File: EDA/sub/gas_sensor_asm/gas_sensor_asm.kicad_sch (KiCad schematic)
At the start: 13 parts, among them IC1 PS1-VOC-1000, U1 SCD43-D-R2, U10 ADS1119IPWR, U11 ADS1119IPWR, U2 SGX-4CO, U3 SGX-4NO2, U4 SGX-4OX, U5 LMP91000SD_NOPB, U6 LMP91000SD_NOPB, U7 LMP91000SD_NOPB, U8 LMP91000SD_NOPB, U9 STM32L031G6U6, Y1 ABS07-32.768KHZ-T

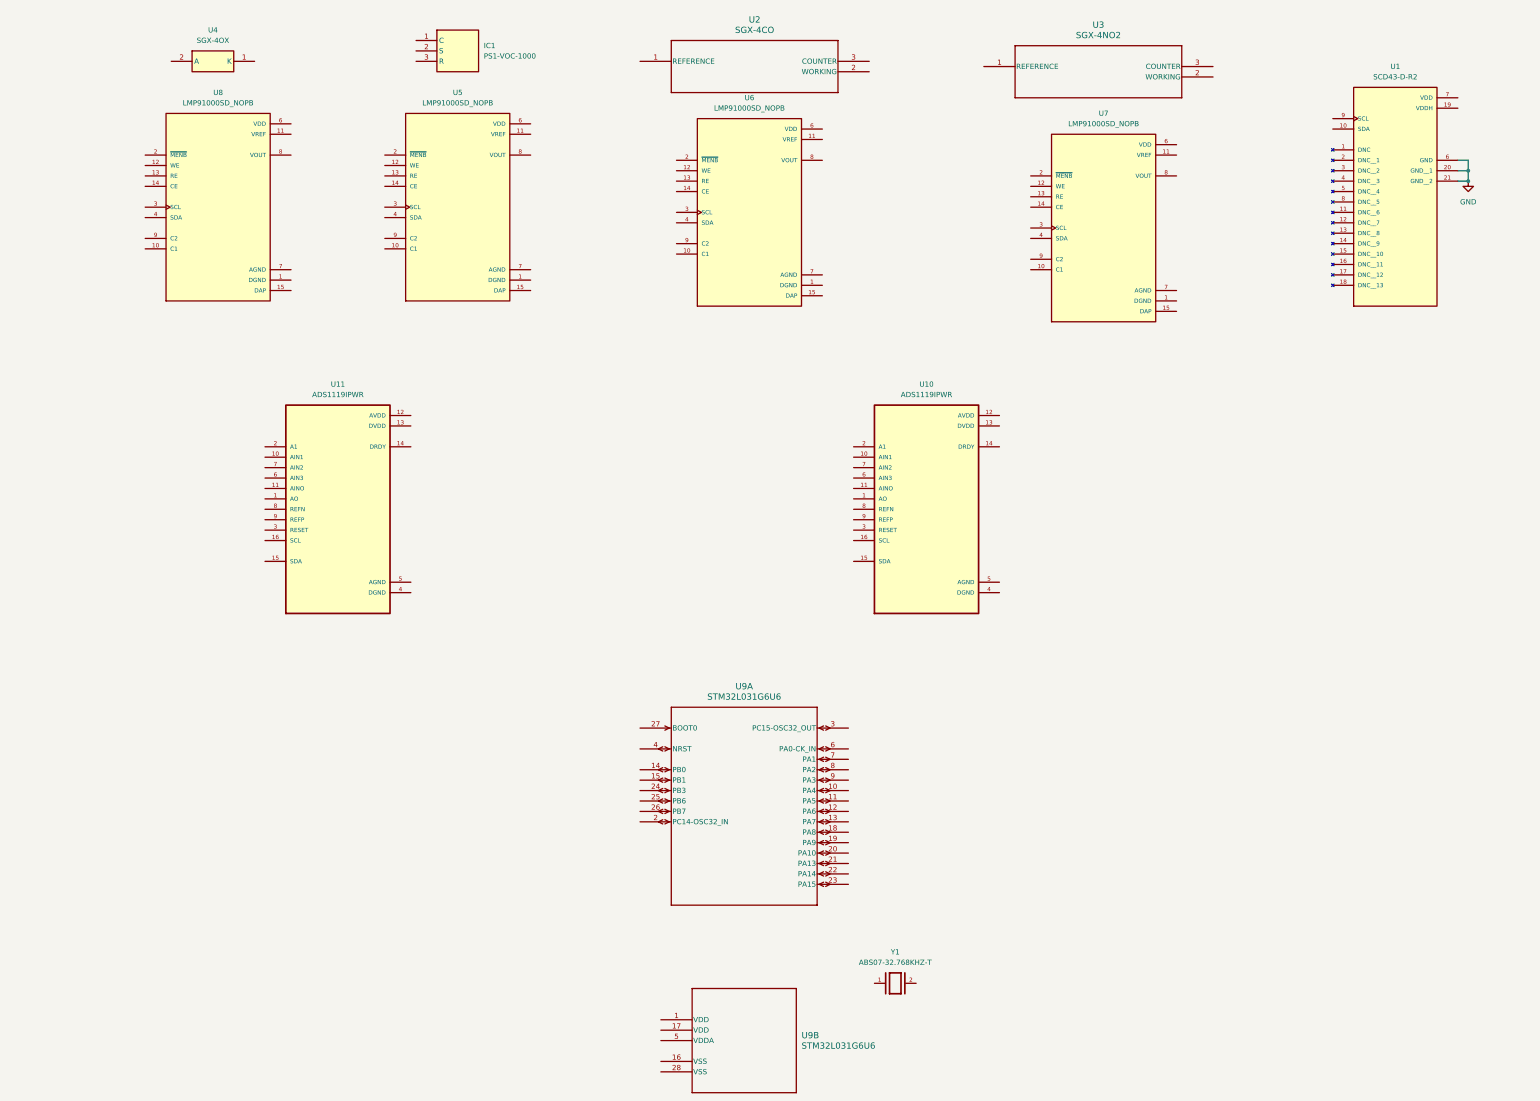
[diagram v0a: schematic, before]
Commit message: Finished gas sensor PCB, and added connector for it on main PCB
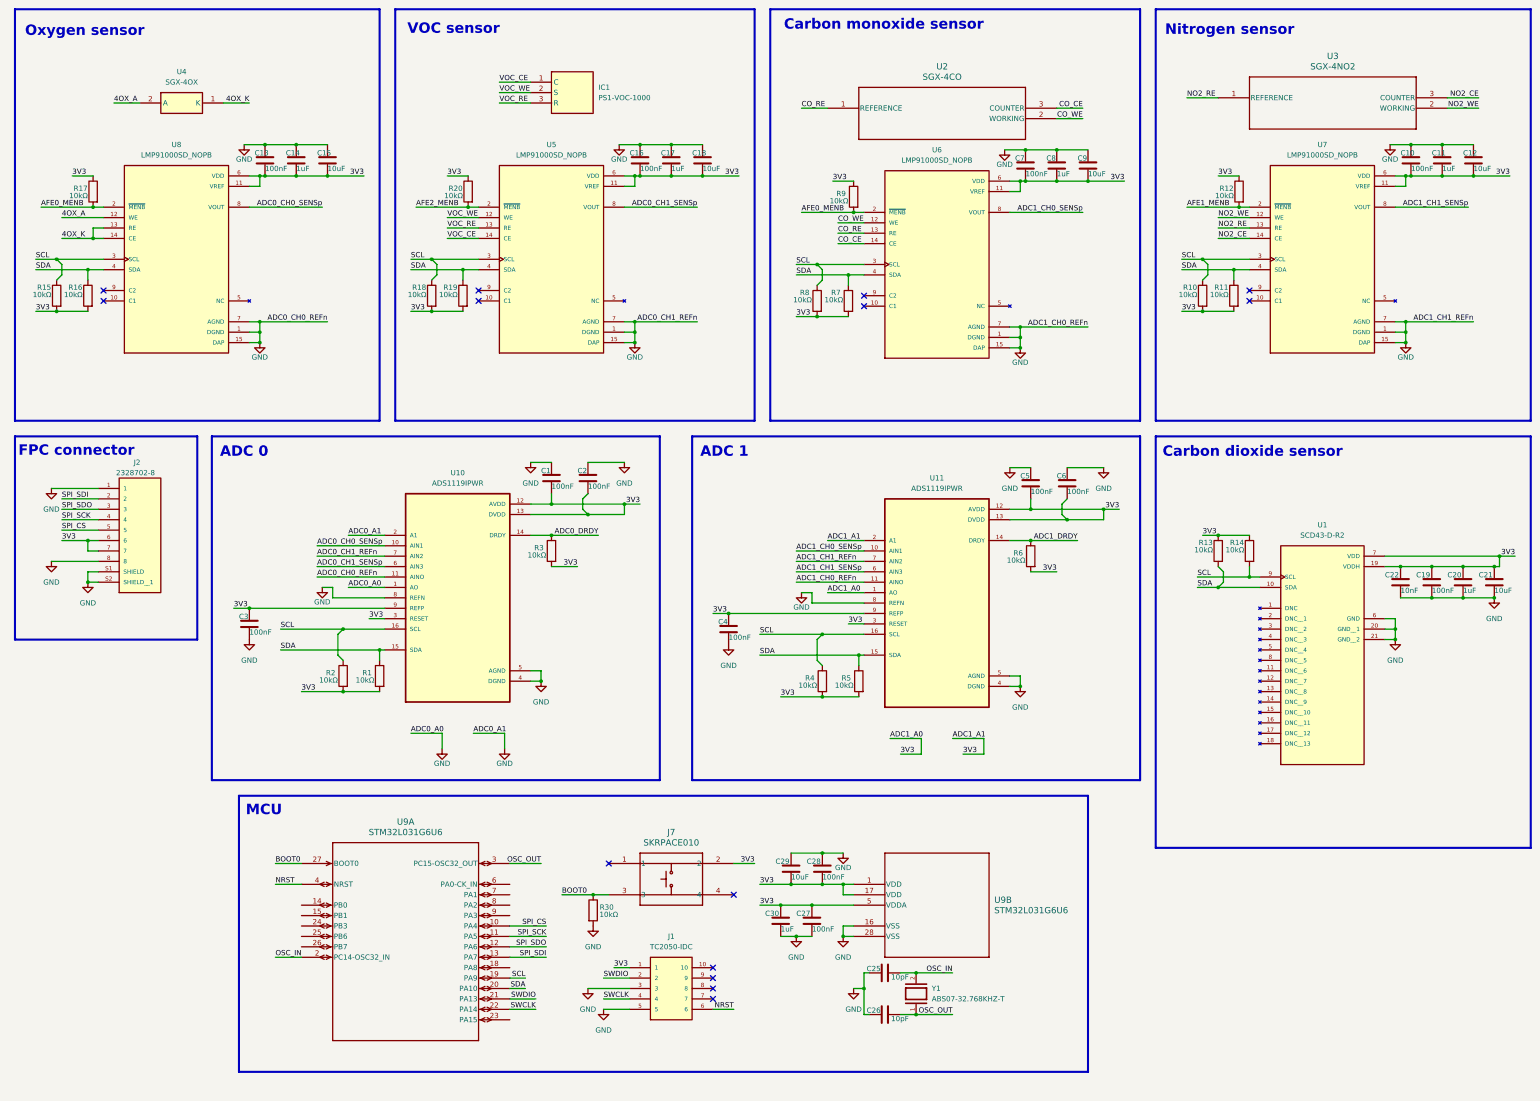
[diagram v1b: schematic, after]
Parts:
- added C1, C10, C13, C16, C19, C2, C27, C28, C3, C4, C5, C6, C7: 100nF, Capacitor_SMD:C_0402_1005Metric, symbol Device:C
- added C11, C14, C17, C20, C30, C8: 1uF, Capacitor_SMD:C_0603_1608Metric, symbol Device:C
- added C12, C15, C18, C21, C29, C9: 10uF, Capacitor_SMD:C_0603_1608Metric, symbol Device:C
- added C22: 10nF, Capacitor_SMD:C_0402_1005Metric, symbol Device:C
- added C25, C26: 10pF, Capacitor_SMD:C_0402_1005Metric, symbol Device:C
- added J1: TC2050-IDC, CANSAT-lib:TAG-CONNECT_TC2050-IDC, symbol CANSAT-lib:TC2050-IDC
- added J2: 2328702-8, CANSAT-lib:TE_2328702-8, symbol CANSAT-lib:2328702-8
- added J7: SKRPACE010, CANSAT-lib:SW_SKRPACE010_AAL, symbol CANSAT-lib:SKRPACE010
- added R1, R10, R11, R12, R13, R14, R15, R16, R17, R18, R19, R2, R20, R3, R30, R4, R5, R6, R7, R8, R9: 10kΩ, Resistor_SMD:R_0402_1005Metric, symbol Device:R
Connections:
- net GND: now also U10.1 (AO), U10.11 (AINO), U10.2 (A1), U10.4 (DGND), U10.5 (AGND), U10.7 (AIN2), U10.8 (REFN), U11.11 (AINO), U11.4 (DGND), U11.5 (AGND), U11.7 (AIN2), U11.8 (REFN), U5.1 (DGND), U5.15 (DAP), U5.7 (AGND), U6.1 (DGND), U6.15 (DAP), U6.7 (AGND), U7.1 (DGND), U7.15 (DAP), U7.7 (AGND), U8.1 (DGND), U8.15 (DAP), U8.7 (AGND), U9.16 (VSS), U9.28 (VSS), C1.1, C10.1, C11.1, C12.1, C13.1, C14.1, C15.1, C16.1, C17.1, C18.1, C19.2, C2.1, C20.2, C21.2, C22.2, C25.1, C26.1, C27.2, C28.1, C29.1, C3.2, C30.2, C4.2, C5.1, C6.1, C7.1, C8.1, C9.1, J1.3, J1.5, J2.1, J2.8, J2.S1 (SHIELD), J2.S2 (SHIELD__1), R30.2
- net 3V3: now reaches U9.1 (VDD)
- net 3V3: now also U1.19 (VDDH), U1.7 (VDD), U10.12 (AVDD), U10.13 (DVDD), U10.3 (RESET), U10.9 (REFP), U11.1 (AO), U11.12 (AVDD), U11.13 (DVDD), U11.2 (A1), U11.3 (RESET), U11.9 (REFP), U5.11 (VREF), U5.6 (VDD), U6.11 (VREF), U6.6 (VDD), U7.11 (VREF), U7.6 (VDD), U8.11 (VREF), U8.6 (VDD), U9.17 (VDD), U9.5 (VDDA), C1.2, C10.2, C11.2, C12.2, C13.2, C14.2, C15.2, C16.2, C17.2, C18.2, C19.1, C2.2, C20.1, C21.1, C22.1, C27.1, C28.2, C29.2, C3.1, C30.1, C4.1, C5.2, C6.2, C7.2, C8.2, C9.2, J1.1, J2.6, J2.7, J7.2, R1.2, R10.2, R11.2, R12.1, R13.1, R14.1, R15.2, R16.2, R17.1, R18.2, R19.2, R2.2, R20.1, R3.2, R4.2, R5.2, R6.2, R7.2, R8.2, R9.1
- net CO_RE: now reaches U2.1 (REFERENCE)
- net CO_RE: now also U6.13 (RE)
- net CO_WE: now reaches U2.2 (WORKING)
- net CO_WE: now also U6.12 (WE)
- net CO_CE: now reaches U2.3 (COUNTER)
- net CO_CE: now also U6.14 (CE)
- net VOC_CE: now reaches IC1.1 (C)
- net VOC_CE: now also U5.14 (CE)
- net VOC_WE: now reaches IC1.2 (S)
- net VOC_WE: now also U5.12 (WE)
- net VOC_RE: now reaches IC1.3 (R)
- net VOC_RE: now also U5.13 (RE)
- net AFE0_MENB: now reaches U6.2 (~{MENB})
- net AFE0_MENB: now also U8.2 (~{MENB}), R17.2, R9.2
- net SCL: now reaches U6.3 (SCL)
- net SCL: now also U1.9 (SCL), U10.16 (SCL), U11.16 (SCL), U5.3 (SCL), U7.3 (SCL), U8.3 (SCL), U9.19 (PA9), R10.1, R14.2, R15.1, R18.1, R2.1, R4.1, R8.1
- net SDA: now reaches U6.4 (SDA)
- net SDA: now also U1.10 (SDA), U10.15 (SDA), U11.15 (SDA), U5.4 (SDA), U7.4 (SDA), U8.4 (SDA), U9.20 (PA10), R1.1, R11.1, R13.2, R16.1, R19.1, R5.1, R7.1
- net ADC1_CH0_SENSp: now reaches U6.8 (VOUT)
- net ADC1_CH0_SENSp: now also U11.10 (AIN1)
- net NO2_RE: now reaches U3.1 (REFERENCE)
- net NO2_RE: now also U7.13 (RE)
- net NO2_WE: now reaches U3.2 (WORKING)
- net NO2_WE: now also U7.12 (WE)
- net NO2_CE: now reaches U3.3 (COUNTER)
- net NO2_CE: now also U7.14 (CE)
- net SPI_CS: now reaches U9.10 (PA4)
- net SPI_CS: now also J2.5
- net SPI_SCK: now reaches U9.11 (PA5)
- net SPI_SCK: now also J2.4
- net SPI_SDO: now reaches U9.12 (PA6)
- net SPI_SDO: now also J2.3
- net SPI_SDI: now reaches U9.13 (PA7)
- net SPI_SDI: now also J2.2
- net OSC_IN: now reaches U9.2 (PC14-OSC32_IN)
- net OSC_IN: now also Y1.2, C25.2
- net SWDIO: now reaches U9.21 (PA13)
- net SWDIO: now also J1.2
- net SWCLK: now reaches U9.22 (PA14)
- net SWCLK: now also J1.4
- net BOOT0: now reaches U9.27 (BOOT0)
- net BOOT0: now also J7.3, R30.1
- net OSC_OUT: now reaches U9.3 (PC15-OSC32_OUT)
- net OSC_OUT: now also Y1.1, C26.2
- net NRST: now reaches U9.4 (NRST)
- net NRST: now also J1.6
- net AFE2_MENB: now reaches U5.2 (~{MENB})
- net AFE2_MENB: now also R20.2
- net ADC0_CH1_SENSp: now reaches U5.8 (VOUT)
- net ADC0_CH1_SENSp: now also U10.6 (AIN3)
- net ADC0_CH0_SENSp: now reaches U10.10 (AIN1)
- net ADC0_CH0_SENSp: now also U8.8 (VOUT)
- net ADC0_DRDY: now reaches U10.14 (DRDY)
- net ADC0_DRDY: now also R3.1
- net 4OX_A: now reaches U8.12 (WE)
- net 4OX_A: now also U4.2 (A)
- net 4OX_K: now reaches U8.13 (RE)
- net 4OX_K: now also U4.1 (K), U8.14 (CE)
- net ADC1_DRDY: now reaches U11.14 (DRDY)
- net ADC1_DRDY: now also R6.1
- net ADC1_CH1_SENSp: now reaches U11.6 (AIN3)
- net ADC1_CH1_SENSp: now also U7.8 (VOUT)
- net AFE1_MENB: now reaches U7.2 (~{MENB})
- net AFE1_MENB: now also R12.2
- no-connect marks 0 -> 14
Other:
- note added: "ADC 0"
- note added: "ADC 1"
- note added: "Carbon dioxide sensor"
- note added: "Carbon monoxide sensor"
- note added: "FPC connector"
- note added: "MCU"
- note added: "Nitrogen sensor"
- note added: "Oxygen sensor"
- note added: "VOC sensor"
- moved on the sheet: IC1, U1, U10, U2, U3, U4, U9A, U9B

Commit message: Added GNSS and SIM800L
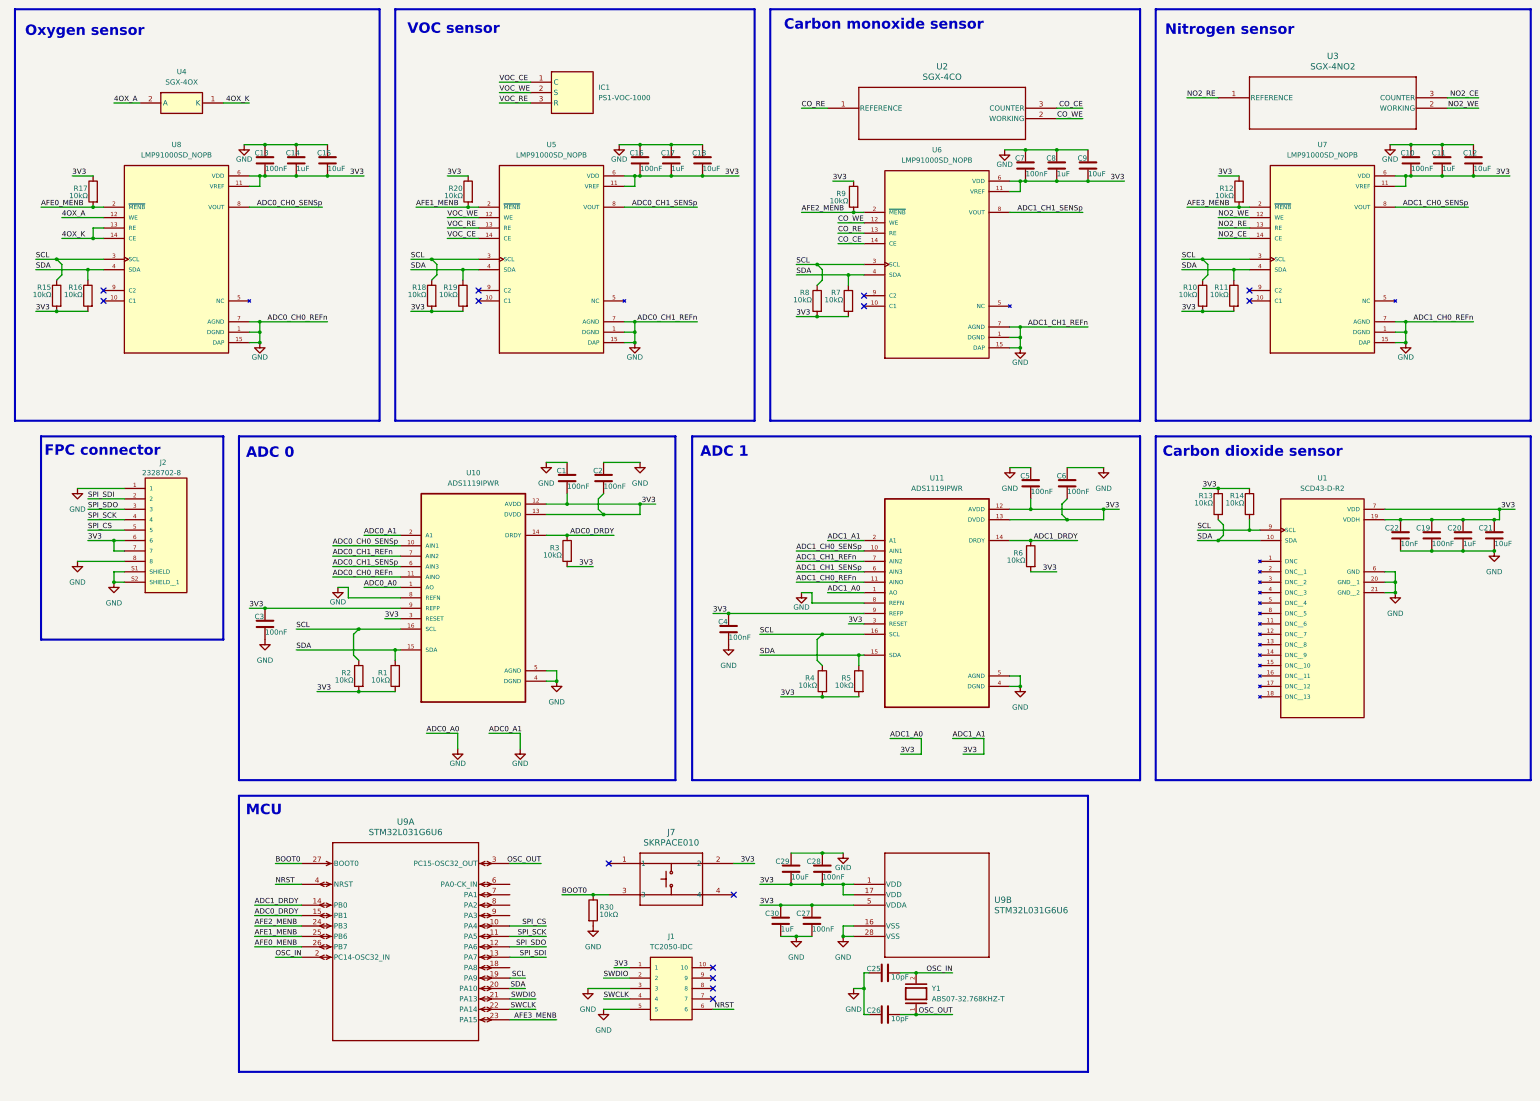
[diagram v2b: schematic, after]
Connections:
- net ADC0_DRDY: now also U9.15 (PB1)
- net ADC1_CH0_SENSp: now also U7.8 (VOUT); no longer U6.8 (VOUT)
- net ADC1_CH1_SENSp: now also U6.8 (VOUT); no longer U7.8 (VOUT)
- net ADC1_DRDY: now also U9.14 (PB0)
- net AFE0_MENB: now also U9.26 (PB7); no longer R9.2, U6.2 (~{MENB})
- net AFE1_MENB: now also R20.2, U5.2 (~{MENB}), U9.25 (PB6); no longer R12.2, U7.2 (~{MENB})
- net AFE2_MENB: now also R9.2, U6.2 (~{MENB}), U9.24 (PB3); no longer R20.2, U5.2 (~{MENB})
- net AFE3_MENB: now reaches U9.23 (PA15)
- net AFE3_MENB: now also R12.2, U7.2 (~{MENB})
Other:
- moved on the sheet: C1, C19, C2, C20, C21, C22, C3, J2, R1, R13, R14, R2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
